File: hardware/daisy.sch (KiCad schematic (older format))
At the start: 8 parts, among them P10 PSOUTH, P11 PEAST, P12 WEST, P13 NORTH, P14 SOUTH, P15 EAST, P8 PWEST, P9 PNORTH

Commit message: Fix silkscreen
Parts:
- P10, P8: footprint Socket_Strips:Socket_Strip_Angled_1x06 -> rgb-matrix:Socket_Strip_Angled_1x06
- P11, P9: footprint Pin_Headers:Pin_Header_Angled_1x06 -> rgb-matrix:Pin_Header_Angled_1x06
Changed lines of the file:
@@
 F 0 "P8" H 3600 4200 50  0000 C CNN
 F 1 "PWEST" V 3700 3800 50  0000 C CNN
-F 2 "Socket_Strips:Socket_Strip_Angled_1x06" H 3600 3800 50  0001 C CNN
+F 2 "rgb-matrix:Socket_Strip_Angled_1x06" H 3600 3800 50  0001 C CNN
 F 3 "" H 3600 3800 50  0000 C CNN
 	1    3600 3800
@@
 F 0 "P11" H 7350 4200 50  0000 C CNN
 F 1 "PEAST" V 7450 3800 50  0000 C CNN
-F 2 "Pin_Headers:Pin_Header_Angled_1x06" H 7350 3800 50  0001 C CNN
+F 2 "rgb-matrix:Pin_Header_Angled_1x06" H 7350 3800 50  0001 C CNN
 F 3 "" H 7350 3800 50  0000 C CNN
 	1    7350 3800
@@
 F 0 "P9" H 5400 2350 50  0000 C CNN
 F 1 "PNORTH" V 5500 1950 50  0000 C CNN
-F 2 "Pin_Headers:Pin_Header_Angled_1x06" H 5400 1950 50  0001 C CNN
+F 2 "rgb-matrix:Pin_Header_Angled_1x06" H 5400 1950 50  0001 C CNN
 F 3 "" H 5400 1950 50  0000 C CNN
 	1    5400 1950
@@
 F 0 "P10" H 5400 6200 50  0000 C CNN
 F 1 "PSOUTH" V 5500 5800 50  0000 C CNN
-F 2 "Socket_Strips:Socket_Strip_Angled_1x06" H 5400 5800 50  0001 C CNN
+F 2 "rgb-matrix:Socket_Strip_Angled_1x06" H 5400 5800 50  0001 C CNN
 F 3 "" H 5400 5800 50  0000 C CNN
 	1    5400 5800

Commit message: Add 2nd GND pin for more curent + minor changes
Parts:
- P10, P8: footprint rgb-matrix:Socket_Strip_Angled_1x06 -> Socket_Strips:Socket_Strip_Angled_1x07; symbol CONN_01X06 -> CONN_01X07
- P11, P9: footprint rgb-matrix:Pin_Header_Angled_1x06 -> Pin_Headers:Pin_Header_Angled_1x07_Pitch2.54mm; symbol CONN_01X06 -> CONN_01X07
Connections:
- wire segments 44 -> 40
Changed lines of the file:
@@
 DATA
 $Comp
-L CONN_01X06 P8
+L CONN_01X07 P8
 U 1 1 581A55CB
-P 3600 3800
-F 0 "P8" H 3600 4200 50  0000 C CNN
-F 1 "PWEST" V 3700 3800 50  0000 C CNN
-F 2 "rgb-matrix:Socket_Strip_Angled_1x06" H 3600 3800 50  0001 C CNN
-F 3 "" H 3600 3800 50  0000 C CNN
-	1    3600 3800
+P 3600 3850
+F 0 "P8" H 3600 4250 50  0000 C CNN
+F 1 "PWEST" V 3700 3850 50  0000 C CNN
+F 2 "Socket_Strips:Socket_Strip_Angled_1x07" H 3600 3850 50  0001 C CNN
+F 3 "" H 3600 3850 50  0000 C CNN
+	1    3600 3850
 	-1   0    0    1
 $EndComp
@@
 L GND #PWR036
 U 1 1 581A55DB
-P 3800 4050
-F 0 "#PWR036" H 3800 3800 50  0001 C CNN
-F 1 "GND" H 3800 3900 50  0000 C CNN
-F 2 "" H 3800 4050 50  0000 C CNN
-F 3 "" H 3800 4050 50  0000 C CNN
-	1    3800 4050
+P 3800 4150
+F 0 "#PWR036" H 3800 3900 50  0001 C CNN
+F 1 "GND" H 3800 4000 50  0000 C CNN
+F 2 "" H 3800 4150 50  0000 C CNN
+F 3 "" H 3800 4150 50  0000 C CNN
+	1    3800 4150
 	-1   0    0    -1
 $EndComp
@@
 DATA
 $Comp
-L CONN_01X06 P11
+L CONN_01X07 P11
 U 1 1 581F606F
-P 7350 3800
-F 0 "P11" H 7350 4200 50  0000 C CNN
-F 1 "PEAST" V 7450 3800 50  0000 C CNN
-F 2 "rgb-matrix:Pin_Header_Angled_1x06" H 7350 3800 50  0001 C CNN
-F 3 "" H 7350 3800 50  0000 C CNN
-	1    7350 3800
+P 7350 3850
+F 0 "P11" H 7350 4250 50  0000 C CNN
+F 1 "PEAST" V 7450 3850 50  0000 C CNN
+F 2 "Pin_Headers:Pin_Header_Angled_1x07_Pitch2.54mm" H 7350 3850 50  0001 C CNN
+F 3 "" H 7350 3850 50  0000 C CNN
+	1    7350 3850
 	1    0    0    1
 $EndComp
@@
 L GND #PWR037
 U 1 1 581F6077
-P 7150 4050
-F 0 "#PWR037" H 7150 3800 50  0001 C CNN
-F 1 "GND" H 7150 3900 50  0000 C CNN
-F 2 "" H 7150 4050 50  0000 C CNN
-F 3 "" H 7150 4050 50  0000 C CNN
-	1    7150 4050
+P 7150 4150
+F 0 "#PWR037" H 7150 3900 50  0001 C CNN
+F 1 "GND" H 7150 4000 50  0000 C CNN
+F 2 "" H 7150 4150 50  0000 C CNN
+F 3 "" H 7150 4150 50  0000 C CNN
+	1    7150 4150
 	1    0    0    -1
 $EndComp
@@
 DATA
 $Comp
-L CONN_01X06 P9
+L CONN_01X07 P9
 U 1 1 581F64E2
-P 5400 1950
-F 0 "P9" H 5400 2350 50  0000 C CNN
-F 1 "PNORTH" V 5500 1950 50  0000 C CNN
-F 2 "rgb-matrix:Pin_Header_Angled_1x06" H 5400 1950 50  0001 C CNN
-F 3 "" H 5400 1950 50  0000 C CNN
-	1    5400 1950
+P 5450 1950
+F 0 "P9" H 5450 2350 50  0000 C CNN
+F 1 "PNORTH" V 5550 1950 50  0000 C CNN
+F 2 "Pin_Headers:Pin_Header_Angled_1x07_Pitch2.54mm" H 5450 1950 50  0001 C CNN
+F 3 "" H 5450 1950 50  0000 C CNN
+	1    5450 1950
 	0    -1   -1   0
 $EndComp
@@
 L GND #PWR038
 U 1 1 581F64EA
-P 5650 2150
-F 0 "#PWR038" H 5650 1900 50  0001 C CNN
-F 1 "GND" H 5650 2000 50  0000 C CNN
-F 2 "" H 5650 2150 50  0000 C CNN
-F 3 "" H 5650 2150 50  0000 C CNN
-	1    5650 2150
+P 5750 2150
+F 0 "#PWR038" H 5750 1900 50  0001 C CNN
+F 1 "GND" H 5750 2000 50  0000 C CNN
+F 2 "" H 5750 2150 50  0000 C CNN
+F 3 "" H 5750 2150 50  0000 C CNN
+	1    5750 2150
 	0    -1   -1   0
 $EndComp
@@
 DATA
 $Comp
-L CONN_01X06 P10
+L CONN_01X07 P10
 U 1 1 581F661C
-P 5400 5800
-F 0 "P10" H 5400 6200 50  0000 C CNN
-F 1 "PSOUTH" V 5500 5800 50  0000 C CNN
-F 2 "rgb-matrix:Socket_Strip_Angled_1x06" H 5400 5800 50  0001 C CNN
-F 3 "" H 5400 5800 50  0000 C CNN
-	1    5400 5800
+P 5450 5800
+F 0 "P10" H 5450 6200 50  0000 C CNN
+F 1 "PSOUTH" V 5550 5800 50  0000 C CNN
+F 2 "Socket_Strips:Socket_Strip_Angled_1x07" H 5450 5800 50  0001 C CNN
+F 3 "" H 5450 5800 50  0000 C CNN
+	1    5450 5800
 	0    -1   1    0
 $EndComp
@@
 L GND #PWR039
 U 1 1 581F6624
-P 5650 5600
-F 0 "#PWR039" H 5650 5350 50  0001 C CNN
-F 1 "GND" H 5650 5450 50  0000 C CNN
-F 2 "" H 5650 5600 50  0000 C CNN
-F 3 "" H 5650 5600 50  0000 C CNN
-	1    5650 5600
+P 5750 5600
+F 0 "#PWR039" H 5750 5350 50  0001 C CNN
+F 1 "GND" H 5750 5450 50  0000 C CNN
+F 2 "" H 5750 5600 50  0000 C CNN
+F 3 "" H 5750 5600 50  0000 C CNN
+	1    5750 5600
 	0    -1   1    0
 $EndComp
@@
 L +5V #PWR040
 U 1 1 584F116F
-P 3850 3500
-F 0 "#PWR040" H 3850 3350 50  0001 C CNN
-F 1 "+5V" H 3850 3640 50  0000 C CNN
-F 2 "" H 3850 3500 50  0000 C CNN
-F 3 "" H 3850 3500 50  0000 C CNN
-	1    3850 3500
+P 3800 3550
+F 0 "#PWR040" H 3800 3400 50  0001 C CNN
+F 1 "+5V" H 3800 3690 50  0000 C CNN
+F 2 "" H 3800 3550 50  0000 C CNN
+F 3 "" H 3800 3550 50  0000 C CNN
+	1    3800 3550
 	1    0    0    -1
 $EndComp
@@
 L +5V #PWR041
 U 1 1 584F18CF
-P 5100 2200
-F 0 "#PWR041" H 5100 2050 50  0001 C CNN
-F 1 "+5V" H 5100 2340 50  0000 C CNN
-F 2 "" H 5100 2200 50  0000 C CNN
-F 3 "" H 5100 2200 50  0000 C CNN
-	1    5100 2200
-	0    -1   -1   0
-$EndComp
-Wire Wire Line
-	4350 3750 4350 3450
-Wire Wire Line
-	4350 4250 4350 3950
-Wire Wire Line
-	3800 3850 4400 3850
-Wire Wire Line
-	3800 3750 4050 3750
-Wire Wire Line
-	3800 3950 4050 3950
-Wire Wire Line
-	2050 2950 1750 2950
-Wire Wire Line
-	2050 2500 1750 2500
-Wire Wire Line
-	2050 2800 1750 2800
-Wire Wire Line
-	2050 2650 1750 2650
-Wire Wire Line
-	7150 3750 6900 3750
-Wire Wire Line
-	7150 3950 6900 3950
-Wire Wire Line
-	7100 3650 7150 3650
-Wire Wire Line
-	7150 3550 7100 3550
-Wire Wire Line
-	5350 2150 5350 2400
-Wire Wire Line
-	5550 2150 5550 2400
-Wire Wire Line
-	5250 2200 5250 2150
-Wire Wire Line
-	5150 2150 5150 2200
-Wire Wire Line
-	5350 5600 5350 5350
-Wire Wire Line
-	5550 5600 5550 5350
-Wire Wire Line
-	5250 5550 5250 5600
-Wire Wire Line
-	5150 5600 5150 5550
-Wire Wire Line
-	4400 3750 4350 3750
-Wire Wire Line
-	4350 3950 4400 3950
-Wire Wire Line
-	5350 5050 5050 5050
-Wire Wire Line
-	5850 5050 5550 5050
-Wire Wire Line
-	5450 5600 5450 5000
-Wire Wire Line
-	5350 5000 5350 5050
-Wire Wire Line
-	5550 5050 5550 5000
-Wire Wire Line
-	6600 3750 6600 3450
-Wire Wire Line
-	6600 4250 6600 3950
-Wire Wire Line
-	7150 3850 6550 3850
-Wire Wire Line
-	6550 3750 6600 3750
-Wire Wire Line
-	6600 3950 6550 3950
-Wire Wire Line
-	5350 2700 5050 2700
-Wire Wire Line
-	5850 2700 5550 2700
-Wire Wire Line
-	5450 2150 5450 2750
-Wire Wire Line
-	5350 2750 5350 2700
-Wire Wire Line
-	5550 2700 5550 2750
-Wire Wire Line
-	3850 3650 3800 3650
-Connection ~ 3850 3550
-Wire Wire Line
-	3850 3550 3800 3550
-Wire Wire Line
-	3850 3500 3850 3650
-Wire Wire Line
-	5100 2200 5250 2200
-Connection ~ 5150 2200
+P 5150 2150
+F 0 "#PWR041" H 5150 2000 50  0001 C CNN
+F 1 "+5V" H 5150 2290 50  0000 C CNN
+F 2 "" H 5150 2150 50  0000 C CNN
+F 3 "" H 5150 2150 50  0000 C CNN
+	1    5150 2150
+	0    -1   -1   0
+$EndComp
 $Comp
 L +5V #PWR042
 U 1 1 584F1DB4
-P 7100 3500
-F 0 "#PWR042" H 7100 3350 50  0001 C CNN
-F 1 "+5V" H 7100 3640 50  0000 C CNN
-F 2 "" H 7100 3500 50  0000 C CNN
-F 3 "" H 7100 3500 50  0000 C CNN
-	1    7100 3500
+P 7150 3550
+F 0 "#PWR042" H 7150 3400 50  0001 C CNN
+F 1 "+5V" H 7150 3690 50  0000 C CNN
+F 2 "" H 7150 3550 50  0000 C CNN
+F 3 "" H 7150 3550 50  0000 C CNN
+	1    7150 3550
 	1    0    0    -1
 $EndComp
-Wire Wire Line
-	7100 3500 7100 3650
-Connection ~ 7100 3550
 $Comp
 L +5V #PWR043
 U 1 1 584F21C6
-P 5100 5550
-F 0 "#PWR043" H 5100 5400 50  0001 C CNN
-F 1 "+5V" H 5100 5690 50  0000 C CNN
-F 2 "" H 5100 5550 50  0000 C CNN
-F 3 "" H 5100 5550 50  0000 C CNN
-	1    5100 5550
-	0    -1   -1   0
-$EndComp
-Wire Wire Line
-	5100 5550 5250 5550
-Connection ~ 5150 5550
+P 5150 5600
+F 0 "#PWR043" H 5150 5450 50  0001 C CNN
+F 1 "+5V" H 5150 5740 50  0000 C CNN
+F 2 "" H 5150 5600 50  0000 C CNN
+F 3 "" H 5150 5600 50  0000 C CNN
+	1    5150 5600
+	0    -1   -1   0
+$EndComp
 Text Notes 2200 3600 0    60   ~ 0
 2x pin headers = 6A max!
+Wire Wire Line
+	4350 3750 4350 3450
+Wire Wire Line
+	4350 4250 4350 3950
+Wire Wire Line
+	3800 3850 4400 3850
+Wire Wire Line
+	3800 3750 4050 3750
+Wire Wire Line
+	3800 3950 4050 3950
+Wire Wire Line
+	2050 2950 1750 2950
+Wire Wire Line
+	2050 2500 1750 2500
+Wire Wire Line
+	2050 2800 1750 2800
+Wire Wire Line
+	2050 2650 1750 2650
+Wire Wire Line
+	7150 3750 6900 3750
+Wire Wire Line
+	7150 3950 6900 3950
+Wire Wire Line
+	5350 2150 5350 2400
+Wire Wire Line
+	5550 2150 5550 2400
+Wire Wire Line
+	5350 5600 5350 5350
+Wire Wire Line
+	5550 5600 5550 5350
+Wire Wire Line
+	4400 3750 4350 3750
+Wire Wire Line
+	4350 3950 4400 3950
+Wire Wire Line
+	5350 5050 5050 5050
+Wire Wire Line
+	5850 5050 5550 5050
+Wire Wire Line
+	5450 5600 5450 5000
+Wire Wire Line
+	5350 5000 5350 5050
+Wire Wire Line
+	5550 5050 5550 5000
+Wire Wire Line
+	6600 3750 6600 3450
+Wire Wire Line
+	6600 4250 6600 3950
+Wire Wire Line
+	7150 3850 6550 3850
+Wire Wire Line
+	6550 3750 6600 3750
+Wire Wire Line
+	6600 3950 6550 3950
+Wire Wire Line
+	5350 2700 5050 2700
+Wire Wire Line
+	5850 2700 5550 2700
+Wire Wire Line
+	5450 2150 5450 2750
+Wire Wire Line
+	5350 2750 5350 2700
+Wire Wire Line
+	5550 2700 5550 2750
+Wire Wire Line
+	3800 4050 3800 4150
+Wire Wire Line
+	5650 5600 5750 5600
+Wire Wire Line
+	5250 5600 5150 5600
+Wire Wire Line
+	3800 3550 3800 3650
+Wire Wire Line
+	5650 2150 5750 2150
+Wire Wire Line
+	5250 2150 5150 2150
+Wire Wire Line
+	7150 4050 7150 4150
+Wire Wire Line
+	7150 3650 7150 3550
 $EndSCHEMATC

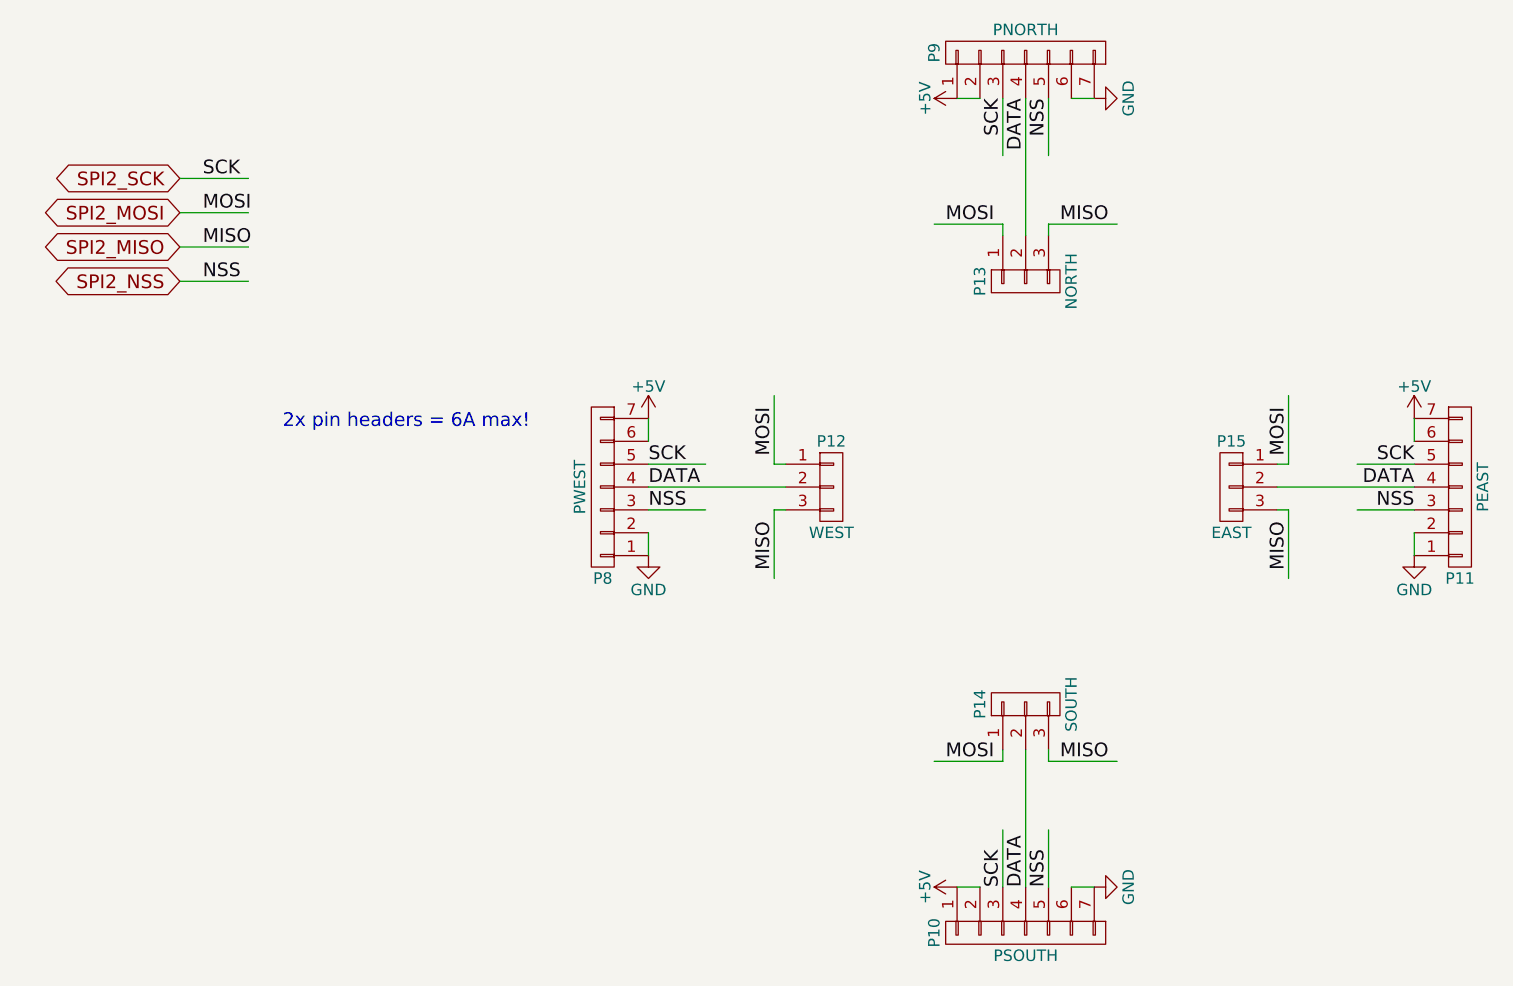
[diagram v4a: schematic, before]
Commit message: PCB fixes for 1.1
* Disconnect DATA lines in daisy chain
* Fix barrel jack footprint (hole size)
* Fix some 3D models
* Update PCB netlist
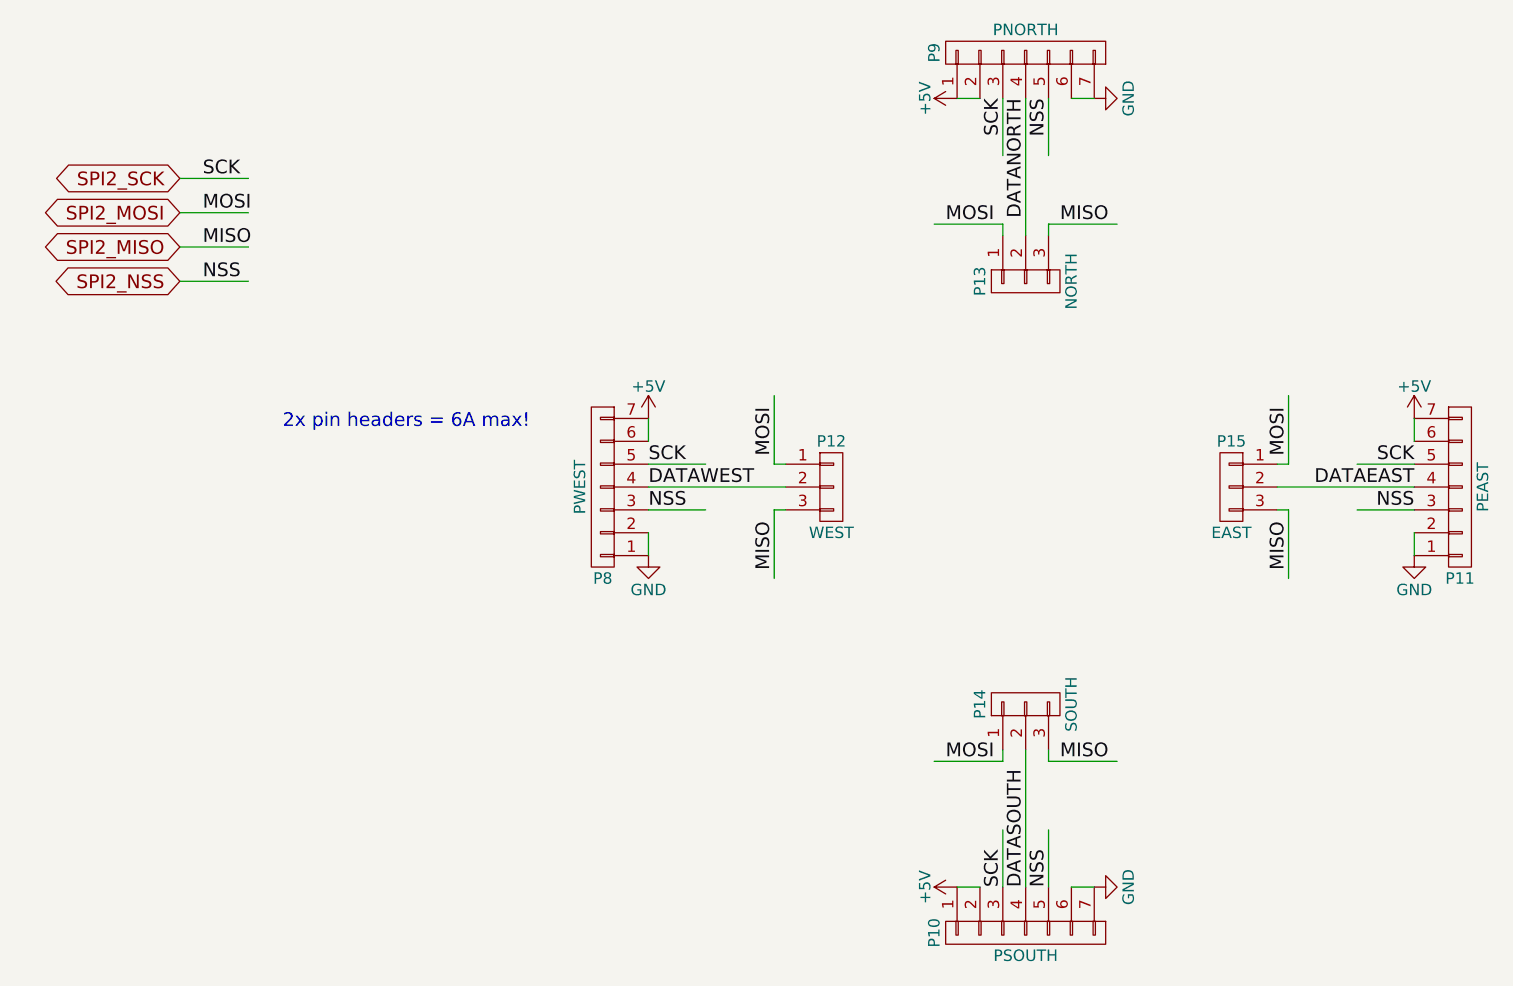
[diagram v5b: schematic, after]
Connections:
- net labels added: DATAEAST, DATANORTH, DATASOUTH, DATAWEST
- net labels removed: DATA
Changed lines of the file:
@@
 SPI2_SCK
 Text Label 3800 3850 0    60   ~ 0
-DATA
+DATAWEST
 $Comp
 L CONN_01X07 P8
@@
 MISO
 $Comp
-L GND #PWR036
+L GND #PWR035
 U 1 1 581A55DB
 P 3800 4150
-F 0 "#PWR036" H 3800 3900 50  0001 C CNN
+F 0 "#PWR035" H 3800 3900 50  0001 C CNN
 F 1 "GND" H 3800 4000 50  0000 C CNN
 F 2 "" H 3800 4150 50  0000 C CNN
@@
 MOSI
 Text Label 7150 3850 2    60   ~ 0
-DATA
+DATAEAST
 $Comp
 L CONN_01X07 P11
@@
 $EndComp
 $Comp
-L GND #PWR037
+L GND #PWR036
 U 1 1 581F6077
 P 7150 4150
-F 0 "#PWR037" H 7150 3900 50  0001 C CNN
+F 0 "#PWR036" H 7150 3900 50  0001 C CNN
 F 1 "GND" H 7150 4000 50  0000 C CNN
 F 2 "" H 7150 4150 50  0000 C CNN
@@
 SCK
 Text Label 5450 2150 3    60   ~ 0
-DATA
+DATANORTH
 $Comp
 L CONN_01X07 P9
@@
 $EndComp
 $Comp
-L GND #PWR038
+L GND #PWR037
 U 1 1 581F64EA
 P 5750 2150
-F 0 "#PWR038" H 5750 1900 50  0001 C CNN
+F 0 "#PWR037" H 5750 1900 50  0001 C CNN
 F 1 "GND" H 5750 2000 50  0000 C CNN
 F 2 "" H 5750 2150 50  0000 C CNN
@@
 SCK
 Text Label 5450 5600 1    60   ~ 0
-DATA
+DATASOUTH
 $Comp
 L CONN_01X07 P10
@@
 $EndComp
 $Comp
-L GND #PWR039
+L GND #PWR038
 U 1 1 581F6624
 P 5750 5600
-F 0 "#PWR039" H 5750 5350 50  0001 C CNN
+F 0 "#PWR038" H 5750 5350 50  0001 C CNN
 F 1 "GND" H 5750 5450 50  0000 C CNN
 F 2 "" H 5750 5600 50  0000 C CNN
@@
 $EndComp
 $Comp
-L +5V #PWR040
+L +5V #PWR039
 U 1 1 584F116F
 P 3800 3550
-F 0 "#PWR040" H 3800 3400 50  0001 C CNN
+F 0 "#PWR039" H 3800 3400 50  0001 C CNN
 F 1 "+5V" H 3800 3690 50  0000 C CNN
 F 2 "" H 3800 3550 50  0000 C CNN
@@
 $EndComp
 $Comp
-L +5V #PWR041
+L +5V #PWR040
 U 1 1 584F18CF
 P 5150 2150
-F 0 "#PWR041" H 5150 2000 50  0001 C CNN
+F 0 "#PWR040" H 5150 2000 50  0001 C CNN
 F 1 "+5V" H 5150 2290 50  0000 C CNN
 F 2 "" H 5150 2150 50  0000 C CNN
@@
 $EndComp
 $Comp
-L +5V #PWR042
+L +5V #PWR041
 U 1 1 584F1DB4
 P 7150 3550
-F 0 "#PWR042" H 7150 3400 50  0001 C CNN
+F 0 "#PWR041" H 7150 3400 50  0001 C CNN
 F 1 "+5V" H 7150 3690 50  0000 C CNN
 F 2 "" H 7150 3550 50  0000 C CNN
@@
 $EndComp
 $Comp
-L +5V #PWR043
+L +5V #PWR042
 U 1 1 584F21C6
 P 5150 5600
-F 0 "#PWR043" H 5150 5450 50  0001 C CNN
+F 0 "#PWR042" H 5150 5450 50  0001 C CNN
 F 1 "+5V" H 5150 5740 50  0000 C CNN
 F 2 "" H 5150 5600 50  0000 C CNN
